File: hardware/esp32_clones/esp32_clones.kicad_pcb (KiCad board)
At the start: 2 copper layers, 110 x 60 mm, 33 parts, among them J2 USB_A, J3 USB_A, J4 USB_A, J5 Micro_SD_Card, J6 Barrel_Jack, J7 DA15_Pins, J9 AudioJack2_Ground

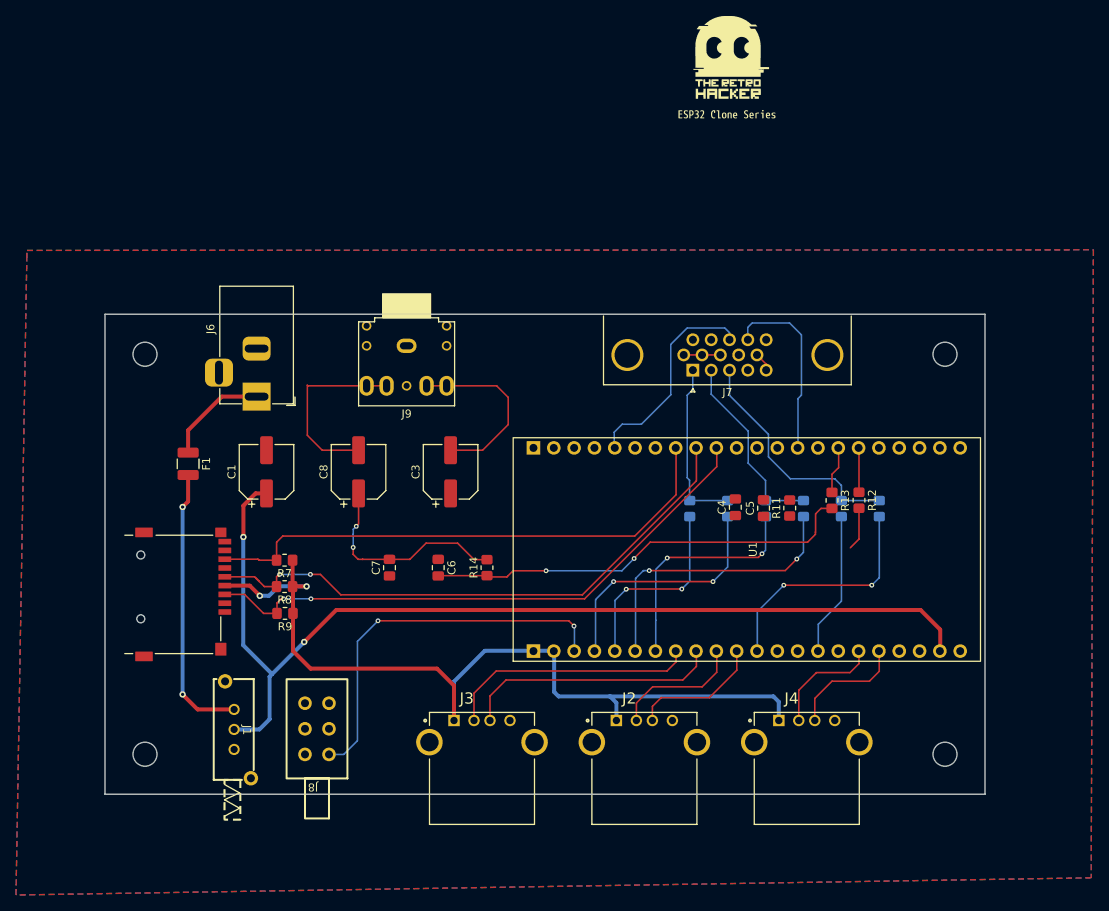
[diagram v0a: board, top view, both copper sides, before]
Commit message: Add production files for ESP32 clones including BOM, designators, netlist, and positions
- Created bom.csv to define components and their specifications.
- Added designators.csv to map designators to their respective values.
- Introduced netlist.ipc for electrical connections and layout.
- Added positions.csv to specify component placements on the PCB.
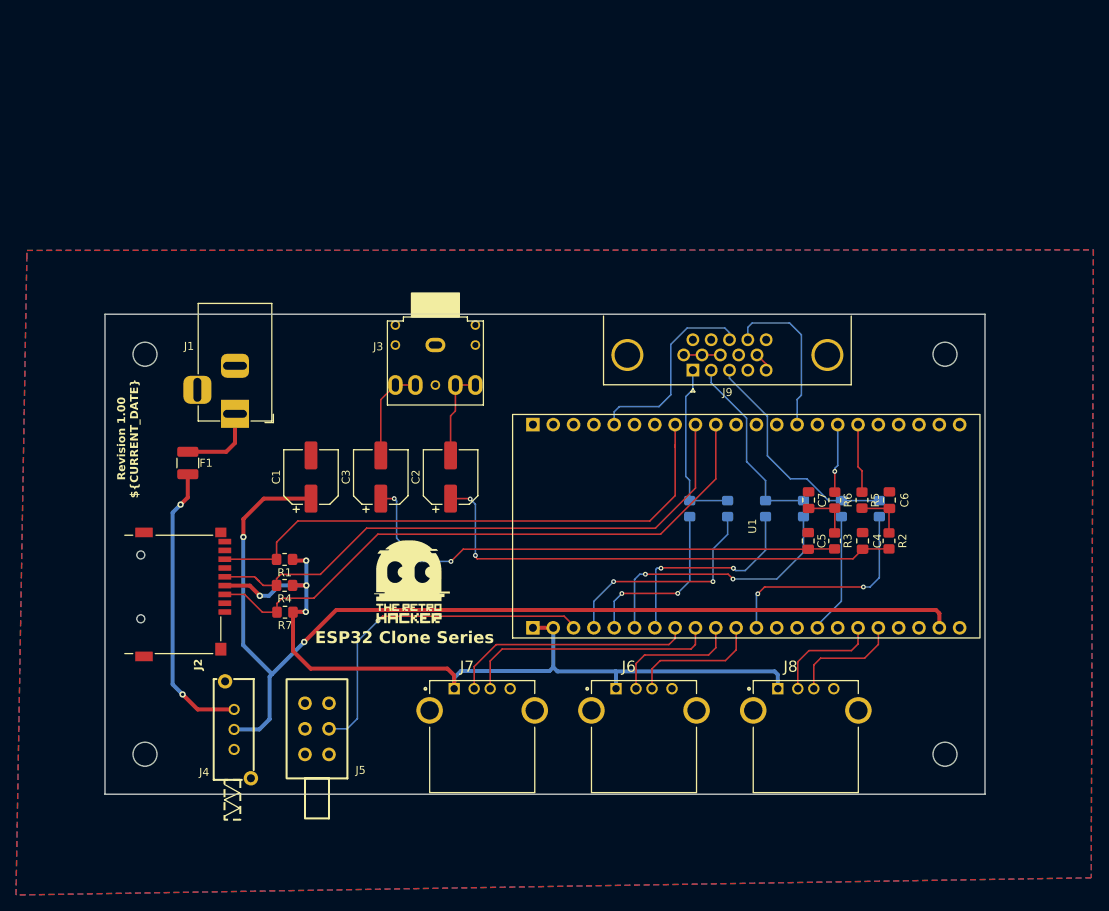
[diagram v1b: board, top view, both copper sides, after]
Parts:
- removed kibuzzard-6A32A25A: G***, kibuzzard-6A32A25A
- R1: renamed from R7; value 10KR -> 10K
- R10: renamed from R3; value 1.2KR -> 1.2K
- R11: renamed from R4; value 560R -> 560
- R12: renamed from R2; value 1.2KR -> 1.2K
- R13: renamed from R1; value 560R -> 560
- R2: renamed from R11; value 330KR -> 330
- R3: renamed from R14; value 330KR -> 330
- R4: renamed from R8; value 10KR -> 10K
- R5: renamed from R12; value 300KR -> 330
- R6: renamed from R13; value 300KR -> 330
- R7: renamed from R9; value 10KR -> 10K
- R8: renamed from R5; value 1.2KR -> 1.2K
- R9: renamed from R6; value 560R -> 560
- moved G*** 76.7 mm to (128.1, 93.8)
- moved C5 52.4 mm to (177.9, 88.3), turned to -90 degrees
- moved C7 47.1 mm to (177.9, 83.2)
- moved R3 43.6 mm to (181.2, 88.3), turned to -90 degrees
- moved C4 16.5 mm to (184.7, 88.3)
- moved C6 15.8 mm to (188.1, 83.2)
- moved R2 13.1 mm to (188.0, 88.3), turned to -90 degrees
- moved C1 5.60 mm to (115.8, 80.3)
- moved J8 3.98 mm to (177.6, 109.5)
- moved J6 3.98 mm to (157.4, 109.5)
- moved J7 3.98 mm to (137.2, 109.5)
- moved J3 3.60 mm to (131.3, 66.8)
- moved J1 3.45 mm to (106.2, 72.5)
- moved U1 2.91 mm to (171.4, 86.5)
- moved C3 2.85 mm to (124.5, 80.3)
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- renumbered C3 to C2, C8 to C3, C7 to C5, C5 to C6, C6 to C7, J6 to J1, J5 to J2, J9 to J3, J1 to J4, J8 to J5, J2 to J6, J3 to J7, J4 to J8, J7 to J9
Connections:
- J5 pad 1: Net-(U1-RST) -> unconnected-(J5-Pad1)
- J5 pad 2: GND -> Net-(U1-RST)
- J5 pad 3: unconnected-(J8-Pad3) -> GND
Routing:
- net Net-(C2-Pad1): track 0.00 -> 62.3 mm, vias 0 -> 2
- net Net-(C7-Pad2): track 54.3 -> 6.40 mm, vias 2 -> 0
- net Net-(C3-Pad1): track 26.6 -> 63.5 mm
- net Net-(C3-Pad2): track 23.4 -> 12.1 mm
- net Net-(C2-Pad2): track 22.7 -> 11.5 mm
- net Net-(U1-RST): track 48.2 -> 42.7 mm
- net +3.3V: track 109.2 -> 104.9 mm, vias 2 -> 4
- net Net-(J2-CMD): track 73.2 -> 76.6 mm, vias 2 -> 0
- net Net-(U1-IO09): track 18.0 -> 14.7 mm
- net Net-(U1-IO07): track 29.1 -> 25.9 mm
- net Net-(F1-Pad1): track 13.1 -> 10.0 mm
- net Net-(U1-IO47): track 5.58 -> 8.64 mm
- net Net-(J2-DAT0): track 67.1 -> 70.0 mm
- net Net-(U1-IO04): track 30.9 -> 28.1 mm
- net Net-(J9-P14): track 23.4 -> 20.5 mm
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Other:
- board text added: "ESP32 Clone Series"
- board text added: "Revision ${REVISION} ${CURRENT_DATE}"

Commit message: Fix to the hardware: VSYNC pin from 0 to 1
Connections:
- U1 pad 19: unconnected-(U1-IO01-Pad19) -> Net-(J9-P14)
- U1 pad 9: Net-(J9-P14) -> unconnected-(U1-IO00-Pad9)
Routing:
- net Net-(J9-P14): track 20.5 -> 30.5 mm
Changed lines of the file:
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@@
 		(title "ESP32 Clones")
 		(date "2026-08-02")
-		(rev "1.00")
+		(rev "1.1")
 		(company "The Retro Hacker")
 		(comment 2 "Commercial-ShareAlike 4.0 Internacional License")
@@
 			(layers "*.Cu" "*.Mask")
 			(remove_unused_layers no)
-			(net "Net-(J9-P14)")
+			(net "unconnected-(U1-IO00-Pad9)")
 			(pinfunction "IO00_9")
-			(pintype "bidirectional")
+			(pintype "bidirectional+no_connect")
 		)
 		(pad "10" thru_hole circle
@@
 			(layers "*.Cu" "*.Mask")
 			(remove_unused_layers no)
-			(net "unconnected-(U1-IO01-Pad19)")
+			(net "Net-(J9-P14)")
 			(pinfunction "IO01_19")
-			(pintype "bidirectional+no_connect")
+			(pintype "bidirectional")
 		)
 		(pad "20" thru_hole circle
@@
 	)
 	(segment
-		(start 177.05 62.575)
-		(end 177.05 70.125)
+		(start 153.65 72.2)
+		(end 153.65 73.8)
 		(width 0.2)
 		(layer "B.Cu")
-		(net "Net-(J9-P14)")
+		(net "Net-(J9-P13)")
 	)
 	(segment
-		(start 175.575 61.1)
-		(end 177.05 62.575)
+		(start 162.775 61.725)
+		(end 160.725 63.775)
 		(width 0.2)
 		(layer "B.Cu")
-		(net "Net-(J9-P14)")
+		(net "Net-(J9-P13)")
 	)
 	(segment
-		(start 170.9 61.1)
-		(end 175.575 61.1)
+		(start 160.725 70.075)
+		(end 159.25 71.55)
 		(width 0.2)
 		(layer "B.Cu")
-		(net "Net-(J9-P14)")
+		(net "Net-(J9-P13)")
 	)
 	(segment
-		(start 170.355 63.19)
-		(end 170.355 61.645)
+		(start 160.725 63.775)
+		(end 160.725 70.075)
 		(width 0.2)
 		(layer "B.Cu")
-		(net "Net-(J9-P14)")
+		(net "Net-(J9-P13)")
 	)
 	(segment
-		(start 177.05 70.125)
-		(end 176.51 70.665)
+		(start 167.475 61.725)
+		(end 162.775 61.725)
 		(width 0.2)
 		(layer "B.Cu")
-		(net "Net-(J9-P14)")
+		(net "Net-(J9-P13)")
 	)
 	(segment
-		(start 176.51 70.665)
-		(end 176.51 73.8)
+		(start 168.065 62.315)
+		(end 167.475 61.725)
 		(width 0.2)
 		(layer "B.Cu")
-		(net "Net-(J9-P14)")
+		(net "Net-(J9-P13)")
 	)
 	(segment
-		(start 170.355 61.645)
-		(end 170.9 61.1)
+		(start 168.065 63.19)
+		(end 168.065 62.315)
 		(width 0.2)
 		(layer "B.Cu")
-		(net "Net-(J9-P14)")
+		(net "Net-(J9-P13)")
 	)
 	(segment
-		(start 160.725 63.775)
-		(end 160.725 70.075)
+		(start 154.3 71.55)
+		(end 153.65 72.2)
 		(width 0.2)
 		(layer "B.Cu")
@@
 	)
 	(segment
-		(start 168.065 62.315)
-		(end 167.475 61.725)
+		(start 160.325 63.609315)
+		(end 160.325 69.275)
 		(width 0.2)
 		(layer "B.Cu")
-		(net "Net-(J9-P13)")
+		(net "Net-(J9-P14)")
 	)
 	(segment
-		(start 167.475 61.725)
-		(end 162.775 61.725)
+		(start 169.375 61.325)
+		(end 162.609314 61.325)
 		(width 0.2)
 		(layer "B.Cu")
-		(net "Net-(J9-P13)")
+		(net "Net-(J9-P14)")
 	)
 	(segment
-		(start 160.725 70.075)
-		(end 159.25 71.55)
+		(start 151.1 71.35)
+		(end 151.1 73.79)
 		(width 0.2)
 		(layer "B.Cu")
-		(net "Net-(J9-P13)")
+		(net "Net-(J9-P14)")
 	)
 	(segment
-		(start 154.3 71.55)
-		(end 153.65 72.2)
+		(start 158.75 70.85)
+		(end 151.6 70.85)
 		(width 0.2)
 		(layer "B.Cu")
-		(net "Net-(J9-P13)")
+		(net "Net-(J9-P14)")
 	)
 	(segment
-		(start 168.065 63.19)
-		(end 168.065 62.315)
+		(start 160.325 69.275)
+		(end 158.75 70.85)
 		(width 0.2)
 		(layer "B.Cu")
-		(net "Net-(J9-P13)")
+		(net "Net-(J9-P14)")
 	)
 	(segment
-		(start 162.775 61.725)
-		(end 160.725 63.775)
+		(start 151.1 73.79)
+		(end 151.11 73.8)
 		(width 0.2)
 		(layer "B.Cu")
-		(net "Net-(J9-P13)")
+		(net "Net-(J9-P14)")
 	)
 	(segment
-		(start 153.65 72.2)
-		(end 153.65 73.8)
+		(start 170.355 63.19)
+		(end 170.355 62.305)
 		(width 0.2)
 		(layer "B.Cu")
-		(net "Net-(J9-P13)")
+		(net "Net-(J9-P14)")
+	)
+	(segment
+		(start 151.6 70.85)
+		(end 151.1 71.35)
+		(width 0.2)
+		(layer "B.Cu")
+		(net "Net-(J9-P14)")
+	)
+	(segment
+		(start 162.609314 61.325)
+		(end 160.325 63.609315)
+		(width 0.2)
+		(layer "B.Cu")
+		(net "Net-(J9-P14)")
+	)
+	(segment
+		(start 170.355 62.305)
+		(end 169.375 61.325)
+		(width 0.2)
+		(layer "B.Cu")
+		(net "Net-(J9-P14)")
 	)
 	(segment

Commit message: - Drove the audio output in stereo, with the left channel on GPIO47 and the right channel on GPIO48. The CP400 sound source is mono, so both channels carry the same signal. - Raised the audio carrier well above the audible range, so the board's audio filter now removes almost all of it instead of leaving an ultrasonic tone on the jack.
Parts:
- C2, C3: footprint Capacitor_SMD:CP_Elec_6.3x3 -> Capacitor_SMD:CP_Elec_5x4.5
- moved G*** 4.68 mm to (123.5, 94.4)
- moved C2 4.10 mm to (129.1, 80.3)
- moved C1 3.38 mm to (112.5, 81.1), turned to 0 degrees
- moved C3 2.77 mm to (121.7, 80.3)
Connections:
- J6 pad 1: +3.3V -> +5V
- J7 pad 1: +3.3V -> +5V
- J8 pad 1: +3.3V -> +5V
- U1 pad 3: unconnected-(U1-IO19-Pad3) -> Net-(J8-D-)
- U1 pad 39: Net-(J8-D-) -> unconnected-(U1-IO11-Pad39)
- U1 pad 4: unconnected-(U1-I020-Pad4) -> Net-(J8-D+)
- U1 pad 40: Net-(J8-D+) -> unconnected-(U1-IO12-Pad40)
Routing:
- net +5V: track 129.8 -> 193.0 mm
- net +3.3V: track 104.9 -> 55.0 mm
- net Net-(J8-D-): track 13.8 -> 48.4 mm, vias 0 -> 1
- net Net-(J8-D+): track 14.2 -> 43.2 mm, vias 0 -> 1
- net Net-(C2-Pad1): track 62.3 -> 66.6 mm
- net Net-(C2-Pad2): track 11.5 -> 15.3 mm
- net Net-(C3-Pad2): track 12.1 -> 15.3 mm
- net Net-(C3-Pad1): track 63.5 -> 66.3 mm

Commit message: - New board and small adjustments for sound on CP400 emulator
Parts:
- removed C3: 10UF, Capacitor_SMD:CP_Elec_5x4.5
- removed C5: 100NF, Capacitor_SMD:C_0805_2012Metric_Pad1.18x1.45mm_HandSolder
- removed C7: 47NF, Capacitor_SMD:C_0805_2012Metric_Pad1.18x1.45mm_HandSolder
- removed R3, R6: 330, Resistor_SMD:R_0805_2012Metric_Pad1.20x1.40mm_HandSolder
- moved C1 3.75 mm to (116.0, 79.9), turned to 90 degrees
- moved C2 3.38 mm to (125.9, 79.2)
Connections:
- J3 pad T: Net-(C3-Pad2) -> Net-(C2-Pad2)
- U1 pad 7: Net-(U1-IO48) -> unconnected-(U1-IO48-Pad7)
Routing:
- net Net-(C3-Pad1): track 66.3 -> 0.00 mm, vias 2 -> 0
- net Net-(C3-Pad2): track 15.3 -> 0.00 mm
- net Net-(U1-IO48): track 8.59 -> 0.00 mm, vias 1 -> 0
- net Net-(C2-Pad2): track 15.3 -> 23.0 mm
- net Net-(C7-Pad2): track 6.40 -> 0.00 mm
- net +5V: track 193.0 -> 197.4 mm
- net Net-(U1-RST): vias 2 -> 1
